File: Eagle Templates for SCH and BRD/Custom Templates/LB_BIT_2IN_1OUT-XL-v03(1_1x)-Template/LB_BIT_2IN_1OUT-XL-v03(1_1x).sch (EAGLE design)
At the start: 22 parts, among them U1 LV321SOT23-5, U2 LV321SOT23-5, U3 LV321SOT23-5

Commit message: Fixed input and output bitsnap connections
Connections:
- removed net SIG_IN: I32BSF1.SIG, I32BSM2.SIG, I?R1.2, I?R2.2, I?R5.2, I?R6.2, I?TVS1.C, I?TVS3.C
- new net SIG1_IN: I32BSM1.SIG, I?R5.2, I?R6.2, I?TVS3.C
- new net SIG2_IN: I32BSM2.SIG, I?R1.2, I?R2.2, I?TVS1.C
- net GND: now also I32BSM1.GND
- net SIG_OUT: now also I32BSF1.SIG
- net VCC: now also I32BSM1.VCC
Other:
- moved on the sheet: I32BSM1, I32BSM2
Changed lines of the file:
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@@
 <part name="U$3" library="LITTLEBITS" deviceset="OSHWCREDIT" device=""/>
 <part name="FRAME1" library="LITTLEBITS" deviceset="FRAME-LETTER" device=""/>
+<part name="P+10" library="SparkFun" deviceset="VCC" device=""/>
+<part name="GND15" library="SparkFun" deviceset="GND" device=""/>
 </parts>
 <sheets>
@@
 <instances>
 <instance part="I32BSF1" gate="G$1" x="226.06" y="162.56"/>
-<instance part="I32BSM1" gate="G$1" x="12.7" y="139.7"/>
-<instance part="I32BSM2" gate="G$1" x="12.7" y="162.56"/>
-<instance part="P+2" gate="1" x="30.48" y="175.26"/>
-<instance part="GND2" gate="1" x="30.48" y="157.48"/>
+<instance part="I32BSM1" gate="G$1" x="17.78" y="165.1"/>
+<instance part="I32BSM2" gate="G$1" x="17.78" y="142.24"/>
+<instance part="P+2" gate="1" x="35.56" y="154.94"/>
+<instance part="GND2" gate="1" x="35.56" y="137.16"/>
 <instance part="U1" gate="G$1" x="53.34" y="78.74" smashed="yes">
 <attribute name="VALUE" x="43.18" y="60.96" size="1.778" layer="96"/>
@@
 <instance part="FRAME1" gate="G$1" x="0" y="0"/>
 <instance part="FRAME1" gate="G$2" x="147.32" y="0"/>
+<instance part="P+10" gate="1" x="35.56" y="175.26"/>
+<instance part="GND15" gate="1" x="35.56" y="162.56"/>
 </instances>
 <busses>
@@
 <segment>
 <pinref part="P+2" gate="1" pin="VCC"/>
-<wire x1="25.4" y1="170.18" x2="30.48" y2="170.18" width="0.1524" layer="91"/>
-<wire x1="30.48" y1="170.18" x2="30.48" y2="175.26" width="0.1524" layer="91"/>
+<wire x1="30.48" y1="149.86" x2="35.56" y2="149.86" width="0.1524" layer="91"/>
+<wire x1="35.56" y1="149.86" x2="35.56" y2="154.94" width="0.1524" layer="91"/>
 <pinref part="I32BSM2" gate="G$1" pin="VCC"/>
 </segment>
@@
 <pinref part="U3" gate="G$1" pin="V+"/>
 <pinref part="P+9" gate="1" pin="VCC"/>
+</segment>
+<segment>
+<pinref part="I32BSM1" gate="G$1" pin="VCC"/>
+<pinref part="P+10" gate="1" pin="VCC"/>
+<wire x1="30.48" y1="172.72" x2="35.56" y2="172.72" width="0.1524" layer="91"/>
+<wire x1="35.56" y1="172.72" x2="35.56" y2="175.26" width="0.1524" layer="91"/>
 </segment>
 </net>
@@
 <segment>
 <pinref part="GND2" gate="1" pin="GND"/>
-<wire x1="25.4" y1="165.1" x2="30.48" y2="165.1" width="0.1524" layer="91"/>
-<wire x1="30.48" y1="165.1" x2="30.48" y2="160.02" width="0.1524" layer="91"/>
+<wire x1="30.48" y1="144.78" x2="35.56" y2="144.78" width="0.1524" layer="91"/>
+<wire x1="35.56" y1="144.78" x2="35.56" y2="139.7" width="0.1524" layer="91"/>
 <pinref part="I32BSM2" gate="G$1" pin="GND"/>
 </segment>
@@
 <pinref part="GND14" gate="1" pin="GND"/>
 <wire x1="20.32" y1="96.52" x2="20.32" y2="93.98" width="0.1524" layer="91"/>
+</segment>
+<segment>
+<pinref part="I32BSM1" gate="G$1" pin="GND"/>
+<pinref part="GND15" gate="1" pin="GND"/>
+<wire x1="30.48" y1="167.64" x2="35.56" y2="167.64" width="0.1524" layer="91"/>
+<wire x1="35.56" y1="167.64" x2="35.56" y2="165.1" width="0.1524" layer="91"/>
 </segment>
 </net>
@@
 </segment>
 </net>
-<net name="SIG_IN" class="0">
-<segment>
-<wire x1="25.4" y1="167.64" x2="30.48" y2="167.64" width="0.1524" layer="91"/>
-<label x="30.48" y="167.64" size="1.778" layer="95" xref="yes"/>
-<pinref part="I32BSM2" gate="G$1" pin="SIG"/>
-</segment>
+<net name="N$4" class="0">
+<segment>
+<pinref part="U1" gate="G$1" pin="+IN"/>
+<pinref part="I?R2" gate="G$1" pin="1"/>
+<wire x1="43.18" y1="81.28" x2="45.72" y2="81.28" width="0.1524" layer="91"/>
+</segment>
+</net>
+<net name="SIG_OUT" class="0">
+<segment>
+<label x="215.9" y="106.68" size="1.778" layer="95" xref="yes"/>
+</segment>
+<segment>
+<pinref part="U2" gate="G$1" pin="-IN"/>
+<wire x1="175.26" y1="104.14" x2="175.26" y2="91.44" width="0.1524" layer="91"/>
+<wire x1="175.26" y1="91.44" x2="190.5" y2="91.44" width="0.1524" layer="91"/>
+<pinref part="U2" gate="G$1" pin="OUT"/>
+<wire x1="190.5" y1="91.44" x2="190.5" y2="106.68" width="0.1524" layer="91"/>
+<wire x1="190.5" y1="106.68" x2="200.66" y2="106.68" width="0.1524" layer="91"/>
+<junction x="190.5" y="106.68"/>
+<pinref part="I?TVS2" gate="G$1" pin="C"/>
+<wire x1="200.66" y1="104.14" x2="200.66" y2="106.68" width="0.1524" layer="91"/>
+<wire x1="215.9" y1="106.68" x2="200.66" y2="106.68" width="0.1524" layer="91"/>
+<junction x="200.66" y="106.68"/>
+</segment>
+<segment>
+<wire x1="223.52" y1="167.64" x2="218.44" y2="167.64" width="0.1524" layer="91"/>
+<label x="218.44" y="167.64" size="1.778" layer="95" rot="R180" xref="yes"/>
+<pinref part="I32BSF1" gate="G$1" pin="SIG"/>
+</segment>
+</net>
+<net name="N$3" class="0">
+<segment>
+<pinref part="U2" gate="G$1" pin="+IN"/>
+<wire x1="175.26" y1="109.22" x2="157.48" y2="109.22" width="0.1524" layer="91"/>
+</segment>
+</net>
+<net name="N$1" class="0">
+<segment>
+<pinref part="U3" gate="G$1" pin="-IN"/>
+<wire x1="45.72" y1="104.14" x2="45.72" y2="91.44" width="0.1524" layer="91"/>
+<wire x1="45.72" y1="91.44" x2="60.96" y2="91.44" width="0.1524" layer="91"/>
+<pinref part="U3" gate="G$1" pin="OUT"/>
+<wire x1="60.96" y1="91.44" x2="60.96" y2="106.68" width="0.1524" layer="91"/>
+<wire x1="60.96" y1="106.68" x2="83.82" y2="106.68" width="0.1524" layer="91"/>
+<junction x="60.96" y="106.68"/>
+</segment>
+</net>
+<net name="N$5" class="0">
+<segment>
+<pinref part="U3" gate="G$1" pin="+IN"/>
+<pinref part="I?R6" gate="G$1" pin="1"/>
+<wire x1="43.18" y1="109.22" x2="45.72" y2="109.22" width="0.1524" layer="91"/>
+</segment>
+</net>
+<net name="SIG1_IN" class="0">
+<segment>
+<label x="15.24" y="109.22" size="1.778" layer="95" rot="R180" xref="yes"/>
+<wire x1="30.48" y1="109.22" x2="33.02" y2="109.22" width="0.1524" layer="91"/>
+<wire x1="15.24" y1="109.22" x2="20.32" y2="109.22" width="0.1524" layer="91"/>
+<wire x1="20.32" y1="109.22" x2="30.48" y2="109.22" width="0.1524" layer="91"/>
+<pinref part="I?R6" gate="G$1" pin="2"/>
+<pinref part="I?TVS3" gate="G$1" pin="C"/>
+<wire x1="30.48" y1="106.68" x2="30.48" y2="109.22" width="0.1524" layer="91"/>
+<junction x="30.48" y="109.22"/>
+<pinref part="I?R5" gate="G$1" pin="2"/>
+<wire x1="20.32" y1="106.68" x2="20.32" y2="109.22" width="0.1524" layer="91"/>
+<junction x="20.32" y="109.22"/>
+</segment>
+<segment>
+<pinref part="I32BSM1" gate="G$1" pin="SIG"/>
+<wire x1="30.48" y1="170.18" x2="35.56" y2="170.18" width="0.1524" layer="91"/>
+<label x="35.56" y="170.18" size="1.778" layer="95" xref="yes"/>
+</segment>
+</net>
+<net name="SIG2_IN" class="0">
 <segment>
 <label x="15.24" y="81.28" size="1.778" layer="95" rot="R180" xref="yes"/>
@@
 </segment>
 <segment>
-<wire x1="223.52" y1="167.64" x2="218.44" y2="167.64" width="0.1524" layer="91"/>
-<label x="218.44" y="167.64" size="1.778" layer="95" rot="R180" xref="yes"/>
-<pinref part="I32BSF1" gate="G$1" pin="SIG"/>
-</segment>
-<segment>
-<label x="15.24" y="109.22" size="1.778" layer="95" rot="R180" xref="yes"/>
-<wire x1="30.48" y1="109.22" x2="33.02" y2="109.22" width="0.1524" layer="91"/>
-<wire x1="15.24" y1="109.22" x2="20.32" y2="109.22" width="0.1524" layer="91"/>
-<wire x1="20.32" y1="109.22" x2="30.48" y2="109.22" width="0.1524" layer="91"/>
-<pinref part="I?R6" gate="G$1" pin="2"/>
-<pinref part="I?TVS3" gate="G$1" pin="C"/>
-<wire x1="30.48" y1="106.68" x2="30.48" y2="109.22" width="0.1524" layer="91"/>
-<junction x="30.48" y="109.22"/>
-<pinref part="I?R5" gate="G$1" pin="2"/>
-<wire x1="20.32" y1="106.68" x2="20.32" y2="109.22" width="0.1524" layer="91"/>
-<junction x="20.32" y="109.22"/>
-</segment>
-</net>
-<net name="N$4" class="0">
-<segment>
-<pinref part="U1" gate="G$1" pin="+IN"/>
-<pinref part="I?R2" gate="G$1" pin="1"/>
-<wire x1="43.18" y1="81.28" x2="45.72" y2="81.28" width="0.1524" layer="91"/>
-</segment>
-</net>
-<net name="SIG_OUT" class="0">
-<segment>
-<label x="215.9" y="106.68" size="1.778" layer="95" xref="yes"/>
-</segment>
-<segment>
-<pinref part="U2" gate="G$1" pin="-IN"/>
-<wire x1="175.26" y1="104.14" x2="175.26" y2="91.44" width="0.1524" layer="91"/>
-<wire x1="175.26" y1="91.44" x2="190.5" y2="91.44" width="0.1524" layer="91"/>
-<pinref part="U2" gate="G$1" pin="OUT"/>
-<wire x1="190.5" y1="91.44" x2="190.5" y2="106.68" width="0.1524" layer="91"/>
-<wire x1="190.5" y1="106.68" x2="200.66" y2="106.68" width="0.1524" layer="91"/>
-<junction x="190.5" y="106.68"/>
-<pinref part="I?TVS2" gate="G$1" pin="C"/>
-<wire x1="200.66" y1="104.14" x2="200.66" y2="106.68" width="0.1524" layer="91"/>
-<wire x1="215.9" y1="106.68" x2="200.66" y2="106.68" width="0.1524" layer="91"/>
-<junction x="200.66" y="106.68"/>
-</segment>
-</net>
-<net name="N$3" class="0">
-<segment>
-<pinref part="U2" gate="G$1" pin="+IN"/>
-<wire x1="175.26" y1="109.22" x2="157.48" y2="109.22" width="0.1524" layer="91"/>
-</segment>
-</net>
-<net name="N$1" class="0">
-<segment>
-<pinref part="U3" gate="G$1" pin="-IN"/>
-<wire x1="45.72" y1="104.14" x2="45.72" y2="91.44" width="0.1524" layer="91"/>
-<wire x1="45.72" y1="91.44" x2="60.96" y2="91.44" width="0.1524" layer="91"/>
-<pinref part="U3" gate="G$1" pin="OUT"/>
-<wire x1="60.96" y1="91.44" x2="60.96" y2="106.68" width="0.1524" layer="91"/>
-<wire x1="60.96" y1="106.68" x2="83.82" y2="106.68" width="0.1524" layer="91"/>
-<junction x="60.96" y="106.68"/>
-</segment>
-</net>
-<net name="N$5" class="0">
-<segment>
-<pinref part="U3" gate="G$1" pin="+IN"/>
-<pinref part="I?R6" gate="G$1" pin="1"/>
-<wire x1="43.18" y1="109.22" x2="45.72" y2="109.22" width="0.1524" layer="91"/>
-</segment>
-</net>
+<wire x1="30.48" y1="147.32" x2="35.56" y2="147.32" width="0.1524" layer="91"/>
+<label x="35.56" y="147.32" size="1.778" layer="95" xref="yes"/>
+<pinref part="I32BSM2" gate="G$1" pin="SIG"/>
+</segment>
+</net>

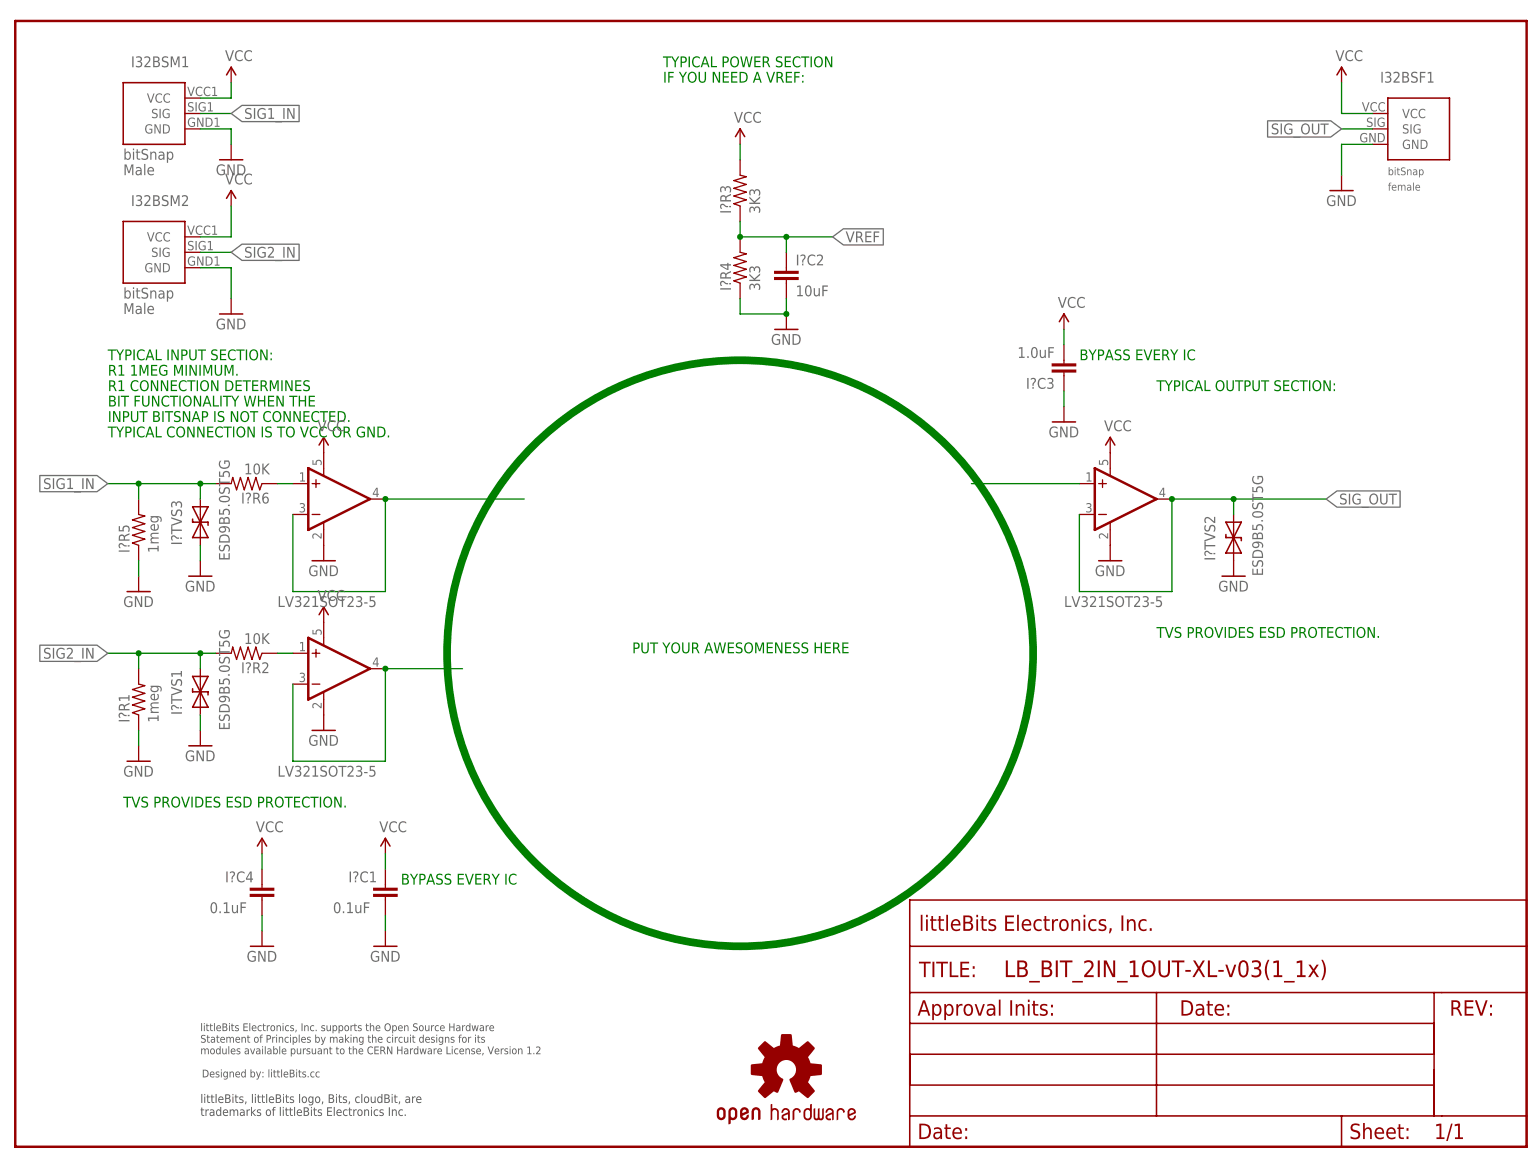
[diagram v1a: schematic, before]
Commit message: Updated templates
- Added ferrite beads
- Moved text and annotations off of Nets layer
- Minor layout changes
- Removed I/O/W prefix from reference designators
- Removed output stage components from output bits
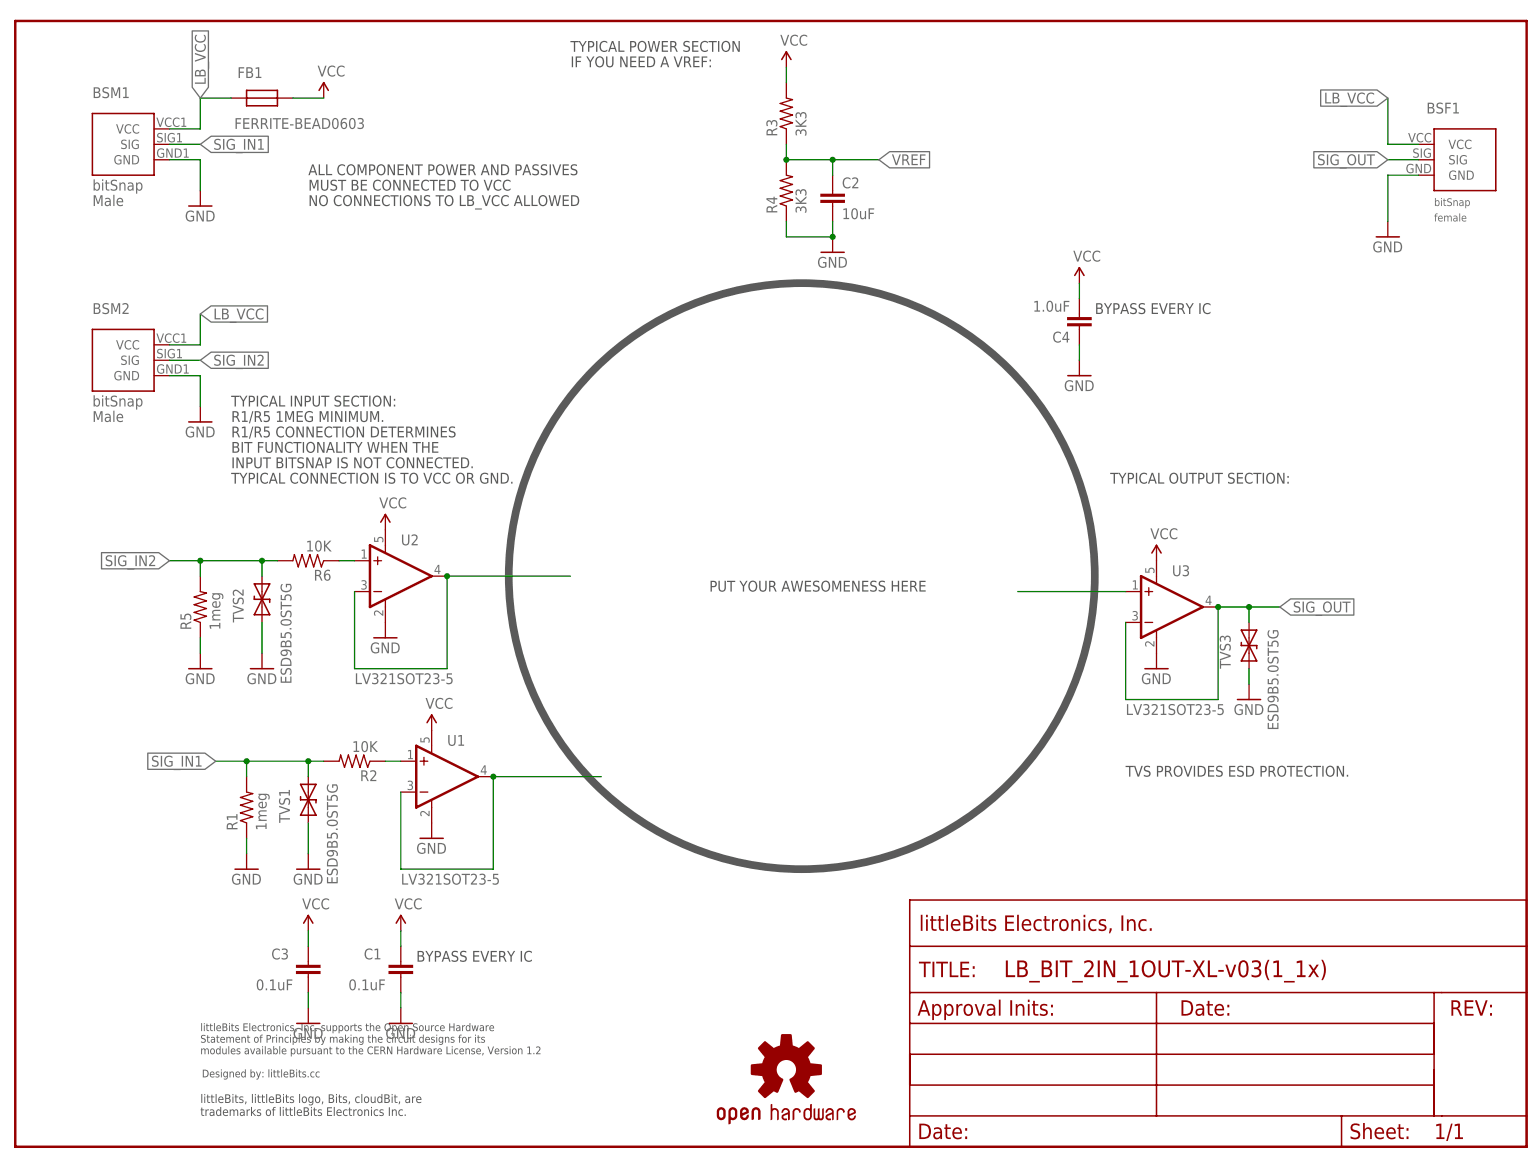
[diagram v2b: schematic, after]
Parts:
- removed I32BSF1: BITSNAP_V03_FEMALE, bitSnap:BITSNAP_V03_FEMALE
- removed I32BSM1, I32BSM2: BITSNAP_V03_MALE, bitSnap:BITSNAP_V03_MALE
- removed I?C1, I?C4: 0.1uF, LITTLEBITS:CAPCAP-0603
- removed I?C2: 10uF, LITTLEBITS:CAPCAP-0603
- removed I?C3: 1.0uF, LITTLEBITS:CAPCAP-0603
- removed I?R1, I?R5: 1meg, LITTLEBITS:RESISTOR0603
- removed I?R2, I?R6: 10K, LITTLEBITS:RESISTOR0603
- removed I?R3, I?R4: 3K3, LITTLEBITS:RESISTOR0603
- removed I?TVS1, I?TVS2, I?TVS3: ESD9B5.0ST5G, LITTLEBITS:DIODE-TVSSOD-923
- added BSF1: BITSNAP_V03_FEMALE, bitSnap:BITSNAP_V03_FEMALE
- added BSM1, BSM2: BITSNAP_V03_MALE, bitSnap:BITSNAP_V03_MALE
- added C1, C3: 0.1uF, LITTLEBITS:CAPCAP-0603
- added C2: 10uF, LITTLEBITS:CAPCAP-0603
- added C4: 1.0uF, LITTLEBITS:CAPCAP-0603
- added FB1: FERRITE-BEAD0603, LITTLEBITS:FERRITE-BEAD0603
- added R1, R5: 1meg, LITTLEBITS:RESISTOR0603
- added R2, R6: 10K, LITTLEBITS:RESISTOR0603
- added R3, R4: 3K3, LITTLEBITS:RESISTOR0603
- added TVS1, TVS2, TVS3: ESD9B5.0ST5G, LITTLEBITS:DIODE-TVSSOD-923
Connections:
- removed net N$3 (its old number): U2.+IN
- removed net N$5: I?R6.1, U3.+IN
- removed net SIG1_IN: I32BSM1.SIG, I?R5.2, I?R6.2, I?TVS3.C
- removed net SIG2_IN: I32BSM2.SIG, I?R1.2, I?R2.2, I?TVS1.C
- new net LB_VCC: BSF1.VCC, BSM1.VCC, BSM2.VCC, FB1.P$2
- new net N$12: U3.+IN
- new net N$2: R6.1, U2.+IN
- new net SIG_IN1: BSM1.SIG, R1.2, R2.2, TVS1.C
- new net SIG_IN2: BSM2.SIG, R5.2, R6.2, TVS2.C
- net GND: now also BSF1.GND, BSM1.GND, BSM2.GND, C1.2, C2.2, C3.2, C4.1, R1.1, R4.1, R5.1, TVS1.A, TVS2.A, TVS3.A; no longer I32BSF1.GND, I32BSM1.GND, I32BSM2.GND, I?C1.2, I?C2.2, I?C3.1, I?C4.2, I?R1.1, I?R4.1, I?R5.1, I?TVS1.A, I?TVS2.A, I?TVS3.A
- net N$1: now also U2.-IN, U2.OUT; no longer U3.-IN, U3.OUT
- net N$4: now also R2.1; no longer I?R2.1
- net SIG_OUT: now also BSF1.SIG, TVS3.C, U3.-IN, U3.OUT; no longer I32BSF1.SIG, I?TVS2.C, U2.-IN, U2.OUT
- net VCC: now also C1.1, C3.1, C4.2, FB1.P$1, R3.2; no longer I32BSF1.VCC, I32BSM1.VCC, I32BSM2.VCC, I?C1.1, I?C3.2, I?C4.1, I?R3.2
- net VREF: now also C2.1, R3.1, R4.2; no longer I?C2.1, I?R3.1, I?R4.2
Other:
- note added: "ALL COMPONENT POWER AND PASSIVES"
- note added: "MUST BE CONNECTED TO VCC"
- note added: "NO CONNECTIONS TO LB_VCC ALLOWED"
- note added: "R1/R5 1MEG MINIMUM."
- note added: "R1/R5 CONNECTION DETERMINES"
- note removed: "R1 1MEG MINIMUM."
- note removed: "R1 CONNECTION DETERMINES"
